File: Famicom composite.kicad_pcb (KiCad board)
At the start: 2 copper layers, 14.2 x 19.9 mm, 11 parts, among them J1 PPU_Pin21, J2 Conn_01x02, J3 Audio_In, J4 Conn_01x04_Female, U1 THS7314

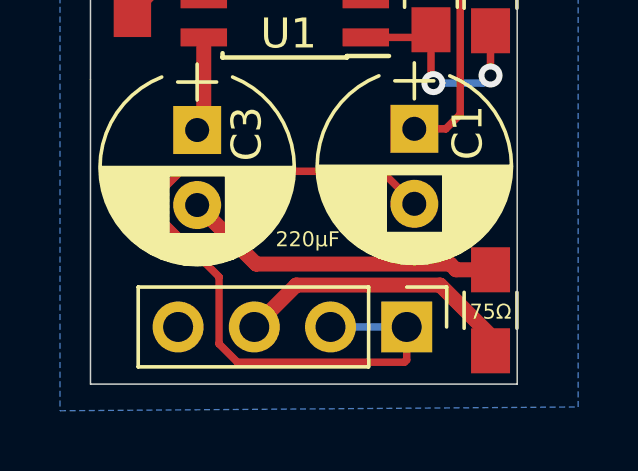
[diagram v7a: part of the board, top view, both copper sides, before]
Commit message: 75ohm pulldown
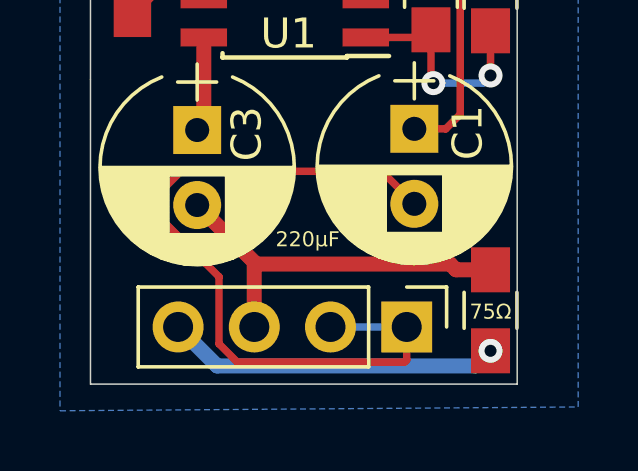
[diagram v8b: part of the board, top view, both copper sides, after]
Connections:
- C3 pad 2: Net-(C3-Pad2) -> /Vid_Out
- R2 pad 1: /Vid_Out -> GND
- R2 pad 2: Net-(C3-Pad2) -> /Vid_Out
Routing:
- net GND: track 9.94 -> 21.1 mm, vias 3 -> 4
- net Net-(C3-Pad2): track 10.7 -> 0.00 mm
- net /Vid_Out: track 9.66 -> 12.8 mm
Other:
- board text added: "fami composite board v0.6"
- board text removed: "fami composite board v0.5"
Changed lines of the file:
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@@
     (thickness 1.6)
     (drawings 20)
-    (tracks 60)
+    (tracks 62)
     (zones 0)
     (modules 11)
-    (nets 12)
+    (nets 11)
   )
   (page A4)
@@
   (net 7 "Net-(C1-Pad2)")
   (net 8 "Net-(C3-Pad1)")
-  (net 9 "Net-(C3-Pad2)")
-  (net 10 "Net-(J1-Pad1)")
-  (net 11 /Half_Vpp)
+  (net 9 "Net-(J1-Pad1)")
+  (net 10 /Half_Vpp)
   (net_class Default "This is the default net class."
     (clearance 0.2)
@@
     (add_net "Net-(C1-Pad2)")
     (add_net "Net-(C3-Pad1)")
-    (add_net "Net-(C3-Pad2)")
     (add_net "Net-(J1-Pad1)")
     (add_net "Net-(U1-Pad6)")
@@
     (fp_line (start -2.075 -2.525) (end -3.475 -2.525) (layer F.SilkS) (width 0.15))
     (pad 1 smd rect (at -2.7 -1.905 180) (size 1.55 0.6) (layers F.Cu F.Paste F.Mask)
-      (net 11 /Half_Vpp))
+      (net 10 /Half_Vpp))
     (pad 2 smd rect (at -2.7 -0.635 180) (size 1.55 0.6) (layers F.Cu F.Paste F.Mask)
       (net 1 GND))
@@
     (fp_line (start 2.35 0.9) (end -2.35 0.9) (layer F.CrtYd) (width 0.05))
     (pad 1 smd rect (at -1.35 0 90) (size 1.5 1.3) (layers F.Cu F.Paste F.Mask)
-      (net 11 /Half_Vpp))
+      (net 10 /Half_Vpp))
     (pad 2 smd rect (at 1.35 0 90) (size 1.5 1.3) (layers F.Cu F.Paste F.Mask)
       (net 1 GND))
@@
     (fp_line (start 2.35 0.9) (end -2.35 0.9) (layer F.CrtYd) (width 0.05))
     (pad 1 smd rect (at -1.35 0 90) (size 1.5 1.3) (layers F.Cu F.Paste F.Mask)
+      (net 1 GND))
+    (pad 2 smd rect (at 1.35 0 90) (size 1.5 1.3) (layers F.Cu F.Paste F.Mask)
       (net 3 /Vid_Out))
-    (pad 2 smd rect (at 1.35 0 90) (size 1.5 1.3) (layers F.Cu F.Paste F.Mask)
-      (net 9 "Net-(C3-Pad2)"))
     (model ${KISYS3DMOD}/Resistors_SMD.3dshapes/R_0805.wrl
       (at (xyz 0 0 0))
@@
     (fp_line (start 2.35 0.9) (end -2.35 0.9) (layer F.CrtYd) (width 0.05))
     (pad 1 smd rect (at -1.35 0 270) (size 1.5 1.3) (layers F.Cu F.Paste F.Mask)
-      (net 10 "Net-(J1-Pad1)"))
+      (net 9 "Net-(J1-Pad1)"))
     (pad 2 smd rect (at 1.35 0 270) (size 1.5 1.3) (layers F.Cu F.Paste F.Mask)
-      (net 11 /Half_Vpp))
+      (net 10 /Half_Vpp))
     (model ${KISYS3DMOD}/Resistors_SMD.3dshapes/R_0805.wrl
       (at (xyz 0 0 0))
@@
     )
     (pad 1 thru_hole rect (at 0 0) (size 1.7 1.7) (drill 1) (layers *.Cu *.Mask)
-      (net 10 "Net-(J1-Pad1)"))
+      (net 9 "Net-(J1-Pad1)"))
     (model ${KISYS3DMOD}/Pin_Headers.3dshapes/Pin_Header_Straight_1x01_Pitch2.54mm.wrl
       (at (xyz 0 0 0))
@@
       (net 8 "Net-(C3-Pad1)"))
     (pad 2 thru_hole circle (at 2.5 0 270) (size 1.6 1.6) (drill 0.8) (layers *.Cu *.Mask)
-      (net 9 "Net-(C3-Pad2)"))
+      (net 3 /Vid_Out))
     (model ${KISYS3DMOD}/Capacitors_THT.3dshapes/CP_Radial_D6.3mm_P2.50mm.wrl
       (at (xyz 0 0 0))
@@
     (effects (font (size 0.6 0.6) (thickness 0.15)) (justify mirror))
   )
-  (gr_text "fami composite board v0.5" (at 128.905 94.869 90) (layer B.SilkS)
+  (gr_text "fami composite board v0.6" (at 128.905 94.869 90) (layer B.SilkS)
     (effects (font (size 0.8 0.8) (thickness 0.15)) (justify mirror))
   )
@@
   (via (at 141.655292 89.607091) (size 0.8) (drill 0.4) (layers F.Cu B.Cu) (net 1))
   (segment (start 141.478 89.784383) (end 141.655292 89.607091) (width 0.5) (layer F.Cu) (net 1))
-  (segment (start 141.478 91.821) (end 141.478 89.784383) (width 0.5) (layer F.Cu) (net 1))
+  (segment (start 141.478 91.821) (end 141.478 89.784383) (width 0.5) (layer F.Cu) (net 1) (status 10))
+  (via (at 141.478 105.189) (size 0.8) (drill 0.4) (layers F.Cu B.Cu) (net 1))
+  (segment (start 132.364001 105.694001) (end 140.972999 105.694001) (width 0.5) (layer B.Cu) (net 1))
+  (segment (start 140.972999 105.694001) (end 141.478 105.189) (width 0.5) (layer B.Cu) (net 1))
+  (segment (start 131.064 104.394) (end 132.364001 105.694001) (width 0.5) (layer B.Cu) (net 1))
   (segment (start 136.845 90.932) (end 137.32 90.932) (width 0.5) (layer F.Cu) (net 2) (status 30))
   (segment (start 134.269001 88.356001) (end 136.845 90.932) (width 0.5) (layer F.Cu) (net 2) (status 20))
@@
   (segment (start 129.54 93.855) (end 130.665 92.73) (width 0.5) (layer F.Cu) (net 2) (status 10))
   (segment (start 129.54 93.98) (end 129.54 93.855) (width 0.5) (layer F.Cu) (net 2) (status 30))
-  (segment (start 135.001 102.997) (end 133.604 104.394) (width 0.5) (layer F.Cu) (net 3) (status 20))
-  (segment (start 141.478 104.677998) (end 139.797002 102.997) (width 0.5) (layer F.Cu) (net 3) (status 10))
-  (segment (start 139.797002 102.997) (end 135.001 102.997) (width 0.5) (layer F.Cu) (net 3))
-  (segment (start 141.478 105.189) (end 141.478 104.677998) (width 0.5) (layer F.Cu) (net 3) (status 30))
   (segment (start 140.468001 97.309999) (end 139.988 97.79) (width 0.25) (layer F.Cu) (net 6))
   (segment (start 140.468001 89.371001) (end 140.468001 97.309999) (width 0.25) (layer F.Cu) (net 6))
@@
   (segment (start 131.92 97.609) (end 131.699 97.83) (width 0.5) (layer F.Cu) (net 8) (status 30))
   (segment (start 131.92 94.742) (end 131.92 97.609) (width 0.5) (layer F.Cu) (net 8) (status 30))
-  (segment (start 133.665989 102.296989) (end 140.135989 102.296989) (width 0.5) (layer F.Cu) (net 9))
-  (segment (start 140.135989 102.296989) (end 140.328 102.489) (width 0.5) (layer F.Cu) (net 9))
-  (segment (start 131.699 100.33) (end 133.665989 102.296989) (width 0.5) (layer F.Cu) (net 9) (status 10))
-  (segment (start 140.328 102.489) (end 141.478 102.489) (width 0.5) (layer F.Cu) (net 9) (status 20))
-  (segment (start 139.493 90.006) (end 139.493 91.788) (width 0.25) (layer F.Cu) (net 10) (status 20))
-  (segment (start 137.752 88.265) (end 139.493 90.006) (width 0.25) (layer F.Cu) (net 10))
-  (segment (start 136.652 88.265) (end 137.752 88.265) (width 0.25) (layer F.Cu) (net 10) (status 10))
-  (segment (start 139.239 94.742) (end 139.493 94.488) (width 0.25) (layer F.Cu) (net 11) (status 30))
-  (segment (start 137.32 94.742) (end 139.239 94.742) (width 0.25) (layer F.Cu) (net 11) (status 30))
-  (via (at 141.478 96.012) (size 0.8) (drill 0.4) (layers F.Cu B.Cu) (net 11))
-  (segment (start 141.478 96.012) (end 141.478 94.521) (width 0.25) (layer F.Cu) (net 11) (status 20))
-  (via (at 139.573 96.266) (size 0.8) (drill 0.4) (layers F.Cu B.Cu) (net 11))
-  (segment (start 139.493 96.186) (end 139.573 96.266) (width 0.25) (layer F.Cu) (net 11))
-  (segment (start 139.493 94.488) (end 139.493 96.186) (width 0.25) (layer F.Cu) (net 11) (status 10))
-  (segment (start 141.224 96.266) (end 141.478 96.012) (width 0.25) (layer B.Cu) (net 11))
-  (segment (start 139.573 96.266) (end 141.224 96.266) (width 0.25) (layer B.Cu) (net 11))
+  (segment (start 133.665989 102.296989) (end 140.135989 102.296989) (width 0.5) (layer F.Cu) (net 3))
+  (segment (start 140.135989 102.296989) (end 140.328 102.489) (width 0.5) (layer F.Cu) (net 3))
+  (segment (start 131.699 100.33) (end 133.665989 102.296989) (width 0.5) (layer F.Cu) (net 3) (status 10))
+  (segment (start 140.328 102.489) (end 141.478 102.489) (width 0.5) (layer F.Cu) (net 3) (status 20))
+  (segment (start 133.604 102.358978) (end 133.604 104.394) (width 0.5) (layer F.Cu) (net 3))
+  (segment (start 133.665989 102.296989) (end 133.604 102.358978) (width 0.5) (layer F.Cu) (net 3))
+  (segment (start 139.493 90.006) (end 139.493 91.788) (width 0.25) (layer F.Cu) (net 9) (status 20))
+  (segment (start 137.752 88.265) (end 139.493 90.006) (width 0.25) (layer F.Cu) (net 9))
+  (segment (start 136.652 88.265) (end 137.752 88.265) (width 0.25) (layer F.Cu) (net 9) (status 10))
+  (segment (start 139.239 94.742) (end 139.493 94.488) (width 0.25) (layer F.Cu) (net 10) (status 30))
+  (segment (start 137.32 94.742) (end 139.239 94.742) (width 0.25) (layer F.Cu) (net 10) (status 30))
+  (via (at 141.478 96.012) (size 0.8) (drill 0.4) (layers F.Cu B.Cu) (net 10))
+  (segment (start 141.478 96.012) (end 141.478 94.521) (width 0.25) (layer F.Cu) (net 10) (status 20))
+  (via (at 139.573 96.266) (size 0.8) (drill 0.4) (layers F.Cu B.Cu) (net 10))
+  (segment (start 139.493 96.186) (end 139.573 96.266) (width 0.25) (layer F.Cu) (net 10))
+  (segment (start 139.493 94.488) (end 139.493 96.186) (width 0.25) (layer F.Cu) (net 10) (status 10))
+  (segment (start 141.224 96.266) (end 141.478 96.012) (width 0.25) (layer B.Cu) (net 10))
+  (segment (start 139.573 96.266) (end 141.224 96.266) (width 0.25) (layer B.Cu) (net 10))
   (zone (net 1) (net_name GND) (layer B.Cu) (hatch edge 0.508)
     (connect_pads (clearance 0.508))
